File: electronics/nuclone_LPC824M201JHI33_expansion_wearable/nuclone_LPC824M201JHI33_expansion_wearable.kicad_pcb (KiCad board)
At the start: 2 copper layers, 45.8 x 25.5 mm, 21 parts, among them J1 nuclone_small_left, J2 nuclone_small_right, J3 DevBoardUartInput, Q1 DMG2305, U1 MCP738312-OT

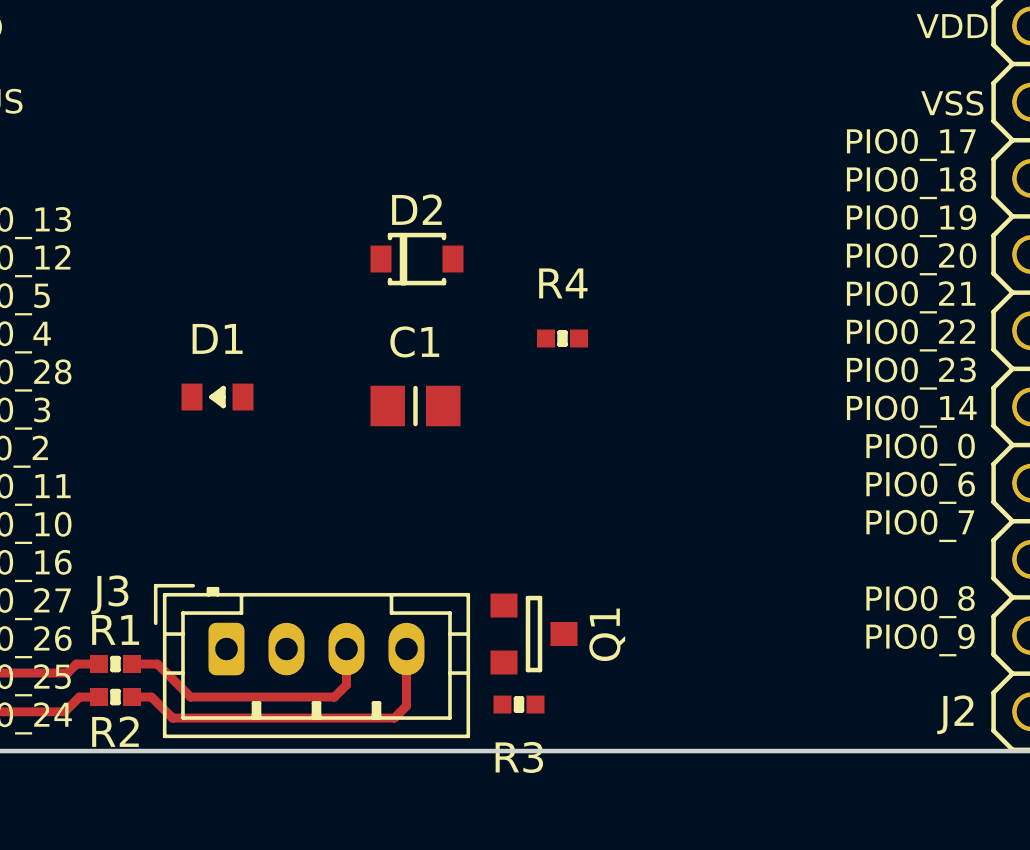
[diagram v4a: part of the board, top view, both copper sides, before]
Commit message: placement of power switching circuit
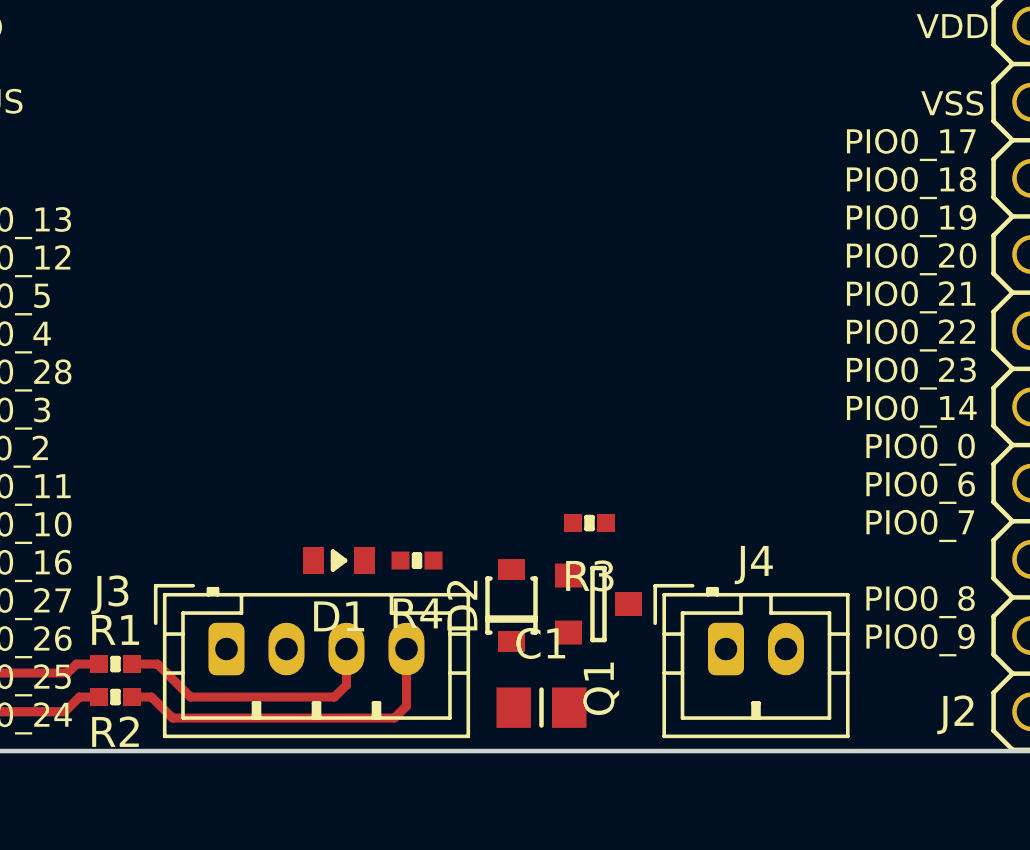
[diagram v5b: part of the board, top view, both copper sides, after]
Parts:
- added J4: batt_recharge, Connector_JST:JST_PH_B2B-PH-K_1x02_P2.00mm_Vertical, F.Cu at (94.0, 95.7)
- moved D2 12.0 mm to (86.8, 94.2), turned to 90 degrees
- moved C1 10.9 mm to (87.8, 97.7)
- moved R4 8.85 mm to (83.7, 92.8), turned to 180 degrees
- moved D1 6.79 mm to (81.0, 92.8), turned to 180 degrees
- moved R3 6.49 mm to (89.4, 91.5)
- moved Q1 2.37 mm to (89.7, 94.2)
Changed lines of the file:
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@@
     (tracks 17)
     (zones 0)
-    (modules 21)
+    (modules 22)
     (nets 42)
   )
@@
     (add_net "Net-(J3-Pad4)")
   )
+  (module Connector_JST:JST_PH_B2B-PH-K_1x02_P2.00mm_Vertical (layer F.Cu)
+    (at 93.95 95.7)
+    (descr "JST PH series connector, B2B-PH-K (http://www.jst-mfg.com/product/pdf/eng/ePH.pdf), generated with kicad-footprint-generator")
+    (tags "connector JST PH side entry")
+    (fp_text reference J4 (at 1 -2.9) (layer F.SilkS)
+      (effects (font (size 1 1) (thickness 0.15)))
+    )
+    (fp_text value batt_recharge (at 1 4) (layer F.Fab)
+      (effects (font (size 1 1) (thickness 0.15)))
+    )
+    (fp_text user %R (at 1 1.5) (layer F.Fab)
+      (effects (font (size 1 1) (thickness 0.15)))
+    )
+    (fp_line (start -2.06 -1.81) (end -2.06 2.91) (layer F.SilkS) (width 0.12))
+    (fp_line (start -2.06 2.91) (end 4.06 2.91) (layer F.SilkS) (width 0.12))
+    (fp_line (start 4.06 2.91) (end 4.06 -1.81) (layer F.SilkS) (width 0.12))
+    (fp_line (start 4.06 -1.81) (end -2.06 -1.81) (layer F.SilkS) (width 0.12))
+    (fp_line (start -0.3 -1.81) (end -0.3 -2.01) (layer F.SilkS) (width 0.12))
+    (fp_line (start -0.3 -2.01) (end -0.6 -2.01) (layer F.SilkS) (width 0.12))
+    (fp_line (start -0.6 -2.01) (end -0.6 -1.81) (layer F.SilkS) (width 0.12))
+    (fp_line (start -0.3 -1.91) (end -0.6 -1.91) (layer F.SilkS) (width 0.12))
+    (fp_line (start 0.5 -1.81) (end 0.5 -1.2) (layer F.SilkS) (width 0.12))
+    (fp_line (start 0.5 -1.2) (end -1.45 -1.2) (layer F.SilkS) (width 0.12))
+    (fp_line (start -1.45 -1.2) (end -1.45 2.3) (layer F.SilkS) (width 0.12))
+    (fp_line (start -1.45 2.3) (end 3.45 2.3) (layer F.SilkS) (width 0.12))
+    (fp_line (start 3.45 2.3) (end 3.45 -1.2) (layer F.SilkS) (width 0.12))
+    (fp_line (start 3.45 -1.2) (end 1.5 -1.2) (layer F.SilkS) (width 0.12))
+    (fp_line (start 1.5 -1.2) (end 1.5 -1.81) (layer F.SilkS) (width 0.12))
+    (fp_line (start -2.06 -0.5) (end -1.45 -0.5) (layer F.SilkS) (width 0.12))
+    (fp_line (start -2.06 0.8) (end -1.45 0.8) (layer F.SilkS) (width 0.12))
+    (fp_line (start 4.06 -0.5) (end 3.45 -0.5) (layer F.SilkS) (width 0.12))
+    (fp_line (start 4.06 0.8) (end 3.45 0.8) (layer F.SilkS) (width 0.12))
+    (fp_line (start 0.9 2.3) (end 0.9 1.8) (layer F.SilkS) (width 0.12))
+    (fp_line (start 0.9 1.8) (end 1.1 1.8) (layer F.SilkS) (width 0.12))
+    (fp_line (start 1.1 1.8) (end 1.1 2.3) (layer F.SilkS) (width 0.12))
+    (fp_line (start 1 2.3) (end 1 1.8) (layer F.SilkS) (width 0.12))
+    (fp_line (start -1.11 -2.11) (end -2.36 -2.11) (layer F.SilkS) (width 0.12))
+    (fp_line (start -2.36 -2.11) (end -2.36 -0.86) (layer F.SilkS) (width 0.12))
+    (fp_line (start -1.11 -2.11) (end -2.36 -2.11) (layer F.Fab) (width 0.1))
+    (fp_line (start -2.36 -2.11) (end -2.36 -0.86) (layer F.Fab) (width 0.1))
+    (fp_line (start -1.95 -1.7) (end -1.95 2.8) (layer F.Fab) (width 0.1))
+    (fp_line (start -1.95 2.8) (end 3.95 2.8) (layer F.Fab) (width 0.1))
+    (fp_line (start 3.95 2.8) (end 3.95 -1.7) (layer F.Fab) (width 0.1))
+    (fp_line (start 3.95 -1.7) (end -1.95 -1.7) (layer F.Fab) (width 0.1))
+    (fp_line (start -2.45 -2.2) (end -2.45 3.3) (layer F.CrtYd) (width 0.05))
+    (fp_line (start -2.45 3.3) (end 4.45 3.3) (layer F.CrtYd) (width 0.05))
+    (fp_line (start 4.45 3.3) (end 4.45 -2.2) (layer F.CrtYd) (width 0.05))
+    (fp_line (start 4.45 -2.2) (end -2.45 -2.2) (layer F.CrtYd) (width 0.05))
+    (pad 2 thru_hole oval (at 2 0) (size 1.2 1.75) (drill 0.75) (layers *.Cu *.Mask)
+      (net 16 /VSS))
+    (pad 1 thru_hole roundrect (at 0 0) (size 1.2 1.75) (drill 0.75) (layers *.Cu *.Mask) (roundrect_rratio 0.208333)
+      (net 36 /VBAT))
+    (model ${KISYS3DMOD}/Connector_JST.3dshapes/JST_PH_B2B-PH-K_1x02_P2.00mm_Vertical.wrl
+      (at (xyz 0 0 0))
+      (scale (xyz 1 1 1))
+      (rotate (xyz 0 0 0))
+    )
+  )
   (module SquantorIC:SOT23-5-Microchip-OT (layer F.Cu)
     (at 81.05 61.6)
@@
   )
   (module SquantorRcl:R_0402_hand (layer F.Cu)
-    (at 88.5 85.35)
+    (at 83.65 92.75 180)
     (descr "Resistor SMD 0402, reflow soldering, Vishay (see dcrcw.pdf)")
     (tags "resistor 0402")
@@
     (fp_line (start -0.1 0.2) (end -0.1 -0.2) (layer F.SilkS) (width 0.15))
     (fp_line (start 0 -0.2) (end 0 0.2) (layer F.SilkS) (width 0.15))
-    (pad 2 smd rect (at 0.55 0) (size 0.6 0.6) (layers F.Cu F.Paste F.Mask)
+    (pad 2 smd rect (at 0.55 0 180) (size 0.6 0.6) (layers F.Cu F.Paste F.Mask)
       (net 38 "Net-(D1-Pad1)"))
-    (pad 1 smd rect (at -0.55 0) (size 0.6 0.6) (layers F.Cu F.Paste F.Mask)
+    (pad 1 smd rect (at -0.55 0 180) (size 0.6 0.6) (layers F.Cu F.Paste F.Mask)
       (net 16 /VSS))
     (model ${KISYS3DMOD}/Resistor_SMD.3dshapes/R_0402_1005Metric.step
@@
   )
   (module SquantorRcl:R_0402_hand (layer F.Cu)
-    (at 87.05 97.55 180)
+    (at 89.4 91.5 180)
     (descr "Resistor SMD 0402, reflow soldering, Vishay (see dcrcw.pdf)")
     (tags "resistor 0402")
@@
   )
   (module SquantorIC:SOT23-3 (layer F.Cu)
-    (at 87.55 95.2 270)
-    (fp_text reference Q1 (at 0 -2.4 90) (layer F.SilkS)
+    (at 89.7 94.2 270)
+    (fp_text reference Q1 (at 2.8 -0.05 90) (layer F.SilkS)
       (effects (font (size 1 1) (thickness 0.15)))
     )
@@
   )
   (module SquantorDiodes:SOD_323_onsemi (layer F.Cu)
-    (at 83.65 82.7)
-    (fp_text reference D2 (at 0 -1.6) (layer F.SilkS)
-      (effects (font (size 1 1) (thickness 0.15)))
-    )
-    (fp_text value NSR0320 (at 0 1.6) (layer F.Fab)
+    (at 86.8 94.25 90)
+    (fp_text reference D2 (at 0 -1.6 90) (layer F.SilkS)
+      (effects (font (size 1 1) (thickness 0.15)))
+    )
+    (fp_text value NSR0320 (at 0 1.6 90) (layer F.Fab)
       (effects (font (size 1 1) (thickness 0.15)))
     )
@@
     (fp_line (start 0.9 0.8) (end 0.9 0.7) (layer F.SilkS) (width 0.15))
     (fp_line (start 0.9 -0.7) (end 0.9 -0.8) (layer F.SilkS) (width 0.15))
-    (pad 2 smd rect (at 1.2 0) (size 0.7 0.9) (layers F.Cu F.Paste F.Mask)
+    (pad 2 smd rect (at 1.2 0 90) (size 0.7 0.9) (layers F.Cu F.Paste F.Mask)
       (net 37 /VUSB))
-    (pad 1 smd rect (at -1.2 0) (size 0.7 0.9) (layers F.Cu F.Paste F.Mask)
+    (pad 1 smd rect (at -1.2 0 90) (size 0.7 0.9) (layers F.Cu F.Paste F.Mask)
       (net 1 /VBUS))
   )
   (module SquantorDiodes:LED_0603_hand (layer F.Cu)
-    (at 77 87.3)
+    (at 81.05 92.75 180)
     (descr "LED SMD 0603, reflow soldering, general purpose")
     (tags "LED 0603")
@@
     (fp_line (start -0.2 0) (end 0.2 0) (layer F.SilkS) (width 0.15))
     (fp_line (start 0.1 -0.2) (end 0.1 0.2) (layer F.SilkS) (width 0.15))
-    (pad 2 smd rect (at 0.85 0) (size 0.7 0.9) (layers F.Cu F.Paste F.Mask)
+    (pad 2 smd rect (at 0.85 0 180) (size 0.7 0.9) (layers F.Cu F.Paste F.Mask)
       (net 37 /VUSB))
-    (pad 1 smd rect (at -0.85 0) (size 0.7 0.9) (layers F.Cu F.Paste F.Mask)
+    (pad 1 smd rect (at -0.85 0 180) (size 0.7 0.9) (layers F.Cu F.Paste F.Mask)
       (net 38 "Net-(D1-Pad1)"))
     (model ${KISYS3DMOD}/LED_SMD.3dshapes/LED_0603_1608Metric.step
@@
   )
   (module SquantorRcl:C_0805+0603 (layer F.Cu)
-    (at 83.6 87.6)
+    (at 87.8 97.65)
     (descr "Capacitor SMD 0805 and 0603 pad sizes, reflow soldering, based on AVX dimensions")
     (tags "capacitor 0805 0603 mixed")
